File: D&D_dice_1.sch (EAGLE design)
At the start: 28 parts, among them IC1 OPA2340U, SW1 SPST_SWITCH, SW2 SPST_SWITCH, SW3 SPST_SWITCH, SW4 SPST_SWITCH, SW5 SPST_SWITCH, SW6 SPST_SWITCH, U1 ATMEGA168

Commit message: Board, code improvement.
Optimized the code, and improved the board a bit.
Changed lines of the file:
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@@
 <instance part="P+4" gate="1" x="132.08" y="154.94"/>
 <instance part="GND6" gate="1" x="45.72" y="144.78"/>
-<instance part="U$3" gate="G$1" x="160.02" y="45.72"/>
+<instance part="U$3" gate="G$1" x="15.24" y="15.24"/>
 <instance part="R15" gate="G$1" x="58.42" y="83.82" rot="R90"/>
 <instance part="GND7" gate="1" x="58.42" y="73.66"/>
@@
 <pinref part="Q1" gate="G$1" pin="B"/>
 <wire x1="10.16" y1="149.86" x2="12.7" y2="147.32" width="0.1524" layer="91"/>
+<junction x="10.16" y="149.86"/>
+<junction x="12.7" y="147.32"/>
 </segment>
 </net>
@@
 <pinref part="GND1" gate="1" pin="GND"/>
 <wire x1="17.78" y1="142.24" x2="17.78" y2="139.7" width="0.1524" layer="91"/>
+<junction x="17.78" y="142.24"/>
+<junction x="17.78" y="139.7"/>
 </segment>
 <segment>
@@
 <pinref part="GND2" gate="1" pin="GND"/>
 <wire x1="50.8" y1="172.72" x2="53.34" y2="172.72" width="0.1524" layer="91"/>
+<junction x="50.8" y="172.72"/>
+<junction x="53.34" y="172.72"/>
 </segment>
 <segment>
@@
 <pinref part="U1" gate="G$1" pin="AGND"/>
 <wire x1="134.62" y1="114.3" x2="134.62" y2="116.84" width="0.1524" layer="91"/>
+<junction x="134.62" y="116.84"/>
+<junction x="134.62" y="114.3"/>
+<junction x="134.62" y="111.76"/>
+<junction x="132.08" y="111.76"/>
 </segment>
 <segment>
@@
 <pinref part="GND6" gate="1" pin="GND"/>
 <wire x1="43.18" y1="147.32" x2="45.72" y2="147.32" width="0.1524" layer="91"/>
+<junction x="43.18" y="147.32"/>
+<junction x="45.72" y="147.32"/>
 </segment>
 <segment>
@@
 <pinref part="C1" gate="G$1" pin="1"/>
 <wire x1="17.78" y1="152.4" x2="22.86" y2="152.4" width="0.1524" layer="91"/>
+<junction x="17.78" y="152.4"/>
+<junction x="22.86" y="152.4"/>
+<junction x="17.78" y="162.56"/>
 </segment>
 </net>
@@
 <pinref part="U$1" gate="G$1" pin="K"/>
 <wire x1="10.16" y1="162.56" x2="10.16" y2="160.02" width="0.1524" layer="91"/>
+<junction x="10.16" y="160.02"/>
+<junction x="10.16" y="162.56"/>
 </segment>
 </net>
@@
 <wire x1="40.64" y1="137.16" x2="35.56" y2="142.24" width="0.1524" layer="91"/>
 <wire x1="35.56" y1="142.24" x2="35.56" y2="152.4" width="0.1524" layer="91"/>
+<junction x="35.56" y="152.4"/>
+<junction x="30.48" y="152.4"/>
+<junction x="38.1" y="152.4"/>
 </segment>
 </net>
@@
 <wire x1="50.8" y1="137.16" x2="55.88" y2="142.24" width="0.1524" layer="91"/>
 <wire x1="55.88" y1="142.24" x2="55.88" y2="154.94" width="0.1524" layer="91"/>
+<junction x="55.88" y="160.02"/>
+<junction x="55.88" y="154.94"/>
 </segment>
 </net>
@@
 <wire x1="38.1" y1="167.64" x2="55.88" y2="167.64" width="0.1524" layer="91"/>
 <wire x1="55.88" y1="167.64" x2="55.88" y2="165.1" width="0.1524" layer="91"/>
+<junction x="38.1" y="167.64"/>
+<junction x="38.1" y="172.72"/>
+<junction x="40.64" y="172.72"/>
+<junction x="55.88" y="165.1"/>
 </segment>
 </net>
@@
 <wire x1="17.78" y1="172.72" x2="27.94" y2="172.72" width="0.1524" layer="91"/>
 <pinref part="SUPPLY1" gate="1" pin="V+"/>
+<junction x="10.16" y="172.72"/>
+<junction x="17.78" y="172.72"/>
+<junction x="27.94" y="172.72"/>
+<junction x="5.08" y="172.72"/>
 </segment>
 <segment>
@@
 <pinref part="IC1" gate="A" pin="V+"/>
 <wire x1="45.72" y1="162.56" x2="43.18" y2="162.56" width="0.1524" layer="91"/>
+<junction x="43.18" y="162.56"/>
+<junction x="45.72" y="162.56"/>
 </segment>
 <segment>
@@
 <pinref part="C2" gate="G$1" pin="2"/>
 <wire x1="124.46" y1="162.56" x2="129.54" y2="162.56" width="0.1524" layer="91"/>
+<junction x="134.62" y="162.56"/>
+<junction x="134.62" y="160.02"/>
+<junction x="134.62" y="157.48"/>
+<junction x="129.54" y="162.56"/>
 </segment>
 <segment>
@@
 <pinref part="P+3" gate="1" pin="V+"/>
 <wire x1="132.08" y1="177.8" x2="134.62" y2="177.8" width="0.1524" layer="91"/>
+<junction x="132.08" y="177.8"/>
+<junction x="134.62" y="177.8"/>
 </segment>
 <segment>
@@
 <pinref part="U1" gate="G$1" pin="PD7(AIN1)"/>
 <wire x1="182.88" y1="127" x2="185.42" y2="127" width="0.1524" layer="91"/>
-<label x="185.42" y="127" size="2.54" layer="95"/>
+<label x="185.42" y="127" size="1.778" layer="95"/>
 </segment>
 </net>
@@
 <wire x1="134.62" y1="167.64" x2="132.08" y2="167.64" width="0.1524" layer="91"/>
 <pinref part="R7" gate="G$1" pin="1"/>
-</segment>
-</net>
+<junction x="132.08" y="167.64"/>
+<junction x="134.62" y="167.64"/>
+</segment>
+</net>

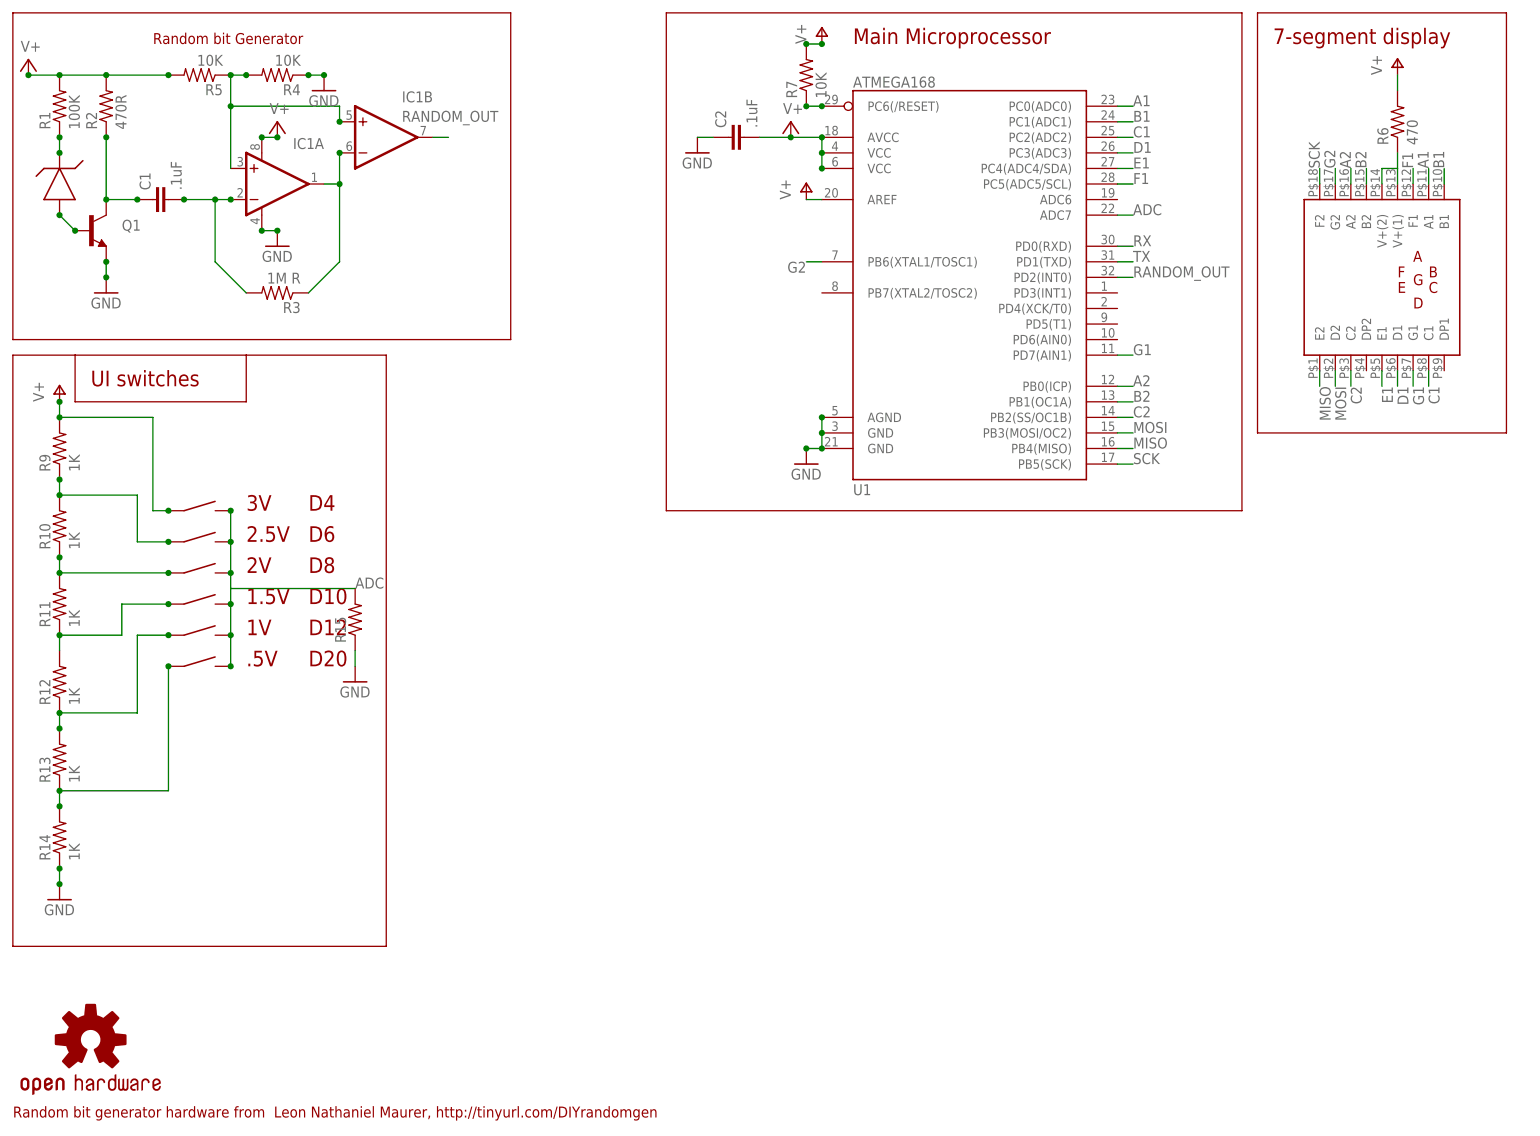
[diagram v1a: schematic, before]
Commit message: Major commit: TESTED
Boards re-jiggered with bigger 0805 pads, because the small ones were
nightmarish. Code also much improved: It now actually works!
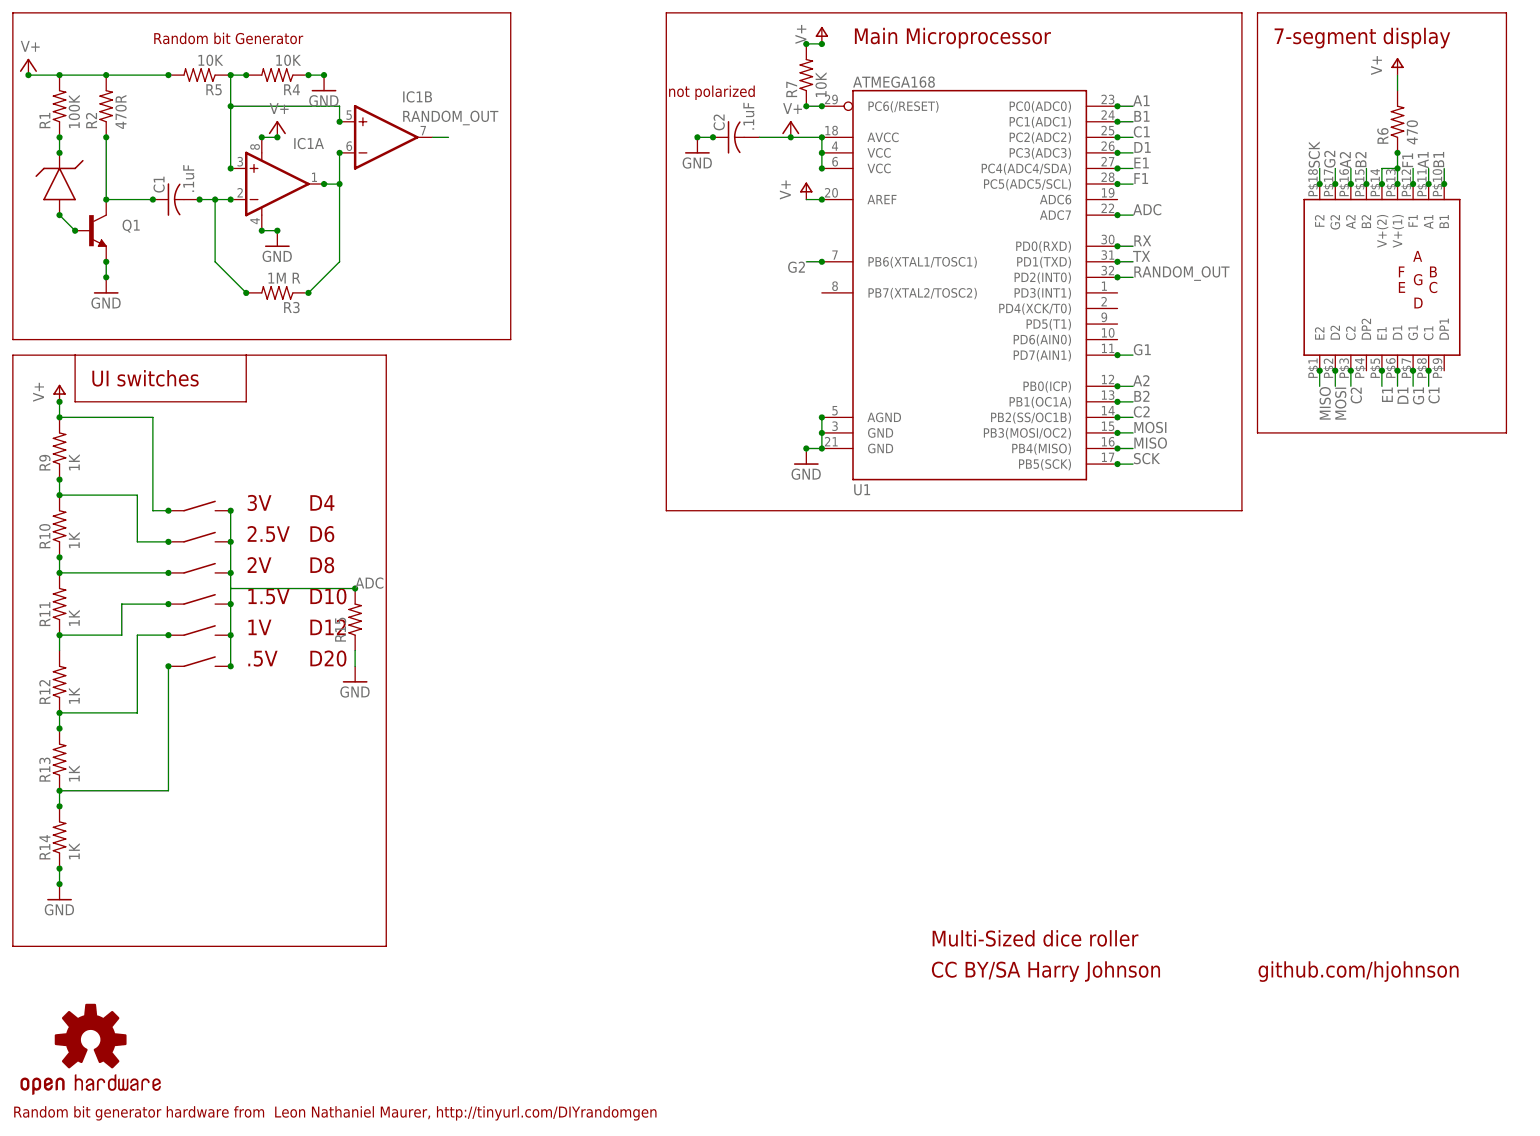
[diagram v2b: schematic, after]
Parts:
- C1, C2: device SparkFun:CAP0805 -> adafruit:C-USC0805
- R1, R10, R11, R12, R13, R14, R15, R2, R4, R5, R6, R7, R9: device SparkFun:RESISTOR0805-RES -> adafruit:R-US_R0805
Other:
- note added: "CC BY/SA Harry Johnson"
- note added: "Multi-Sized dice roller"
- note added: "github.com/hjohnson"
- note added: "not polarized"
- moved on the sheet: C1

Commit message: Added test pads for reset, lightly shifted around a few resistors.
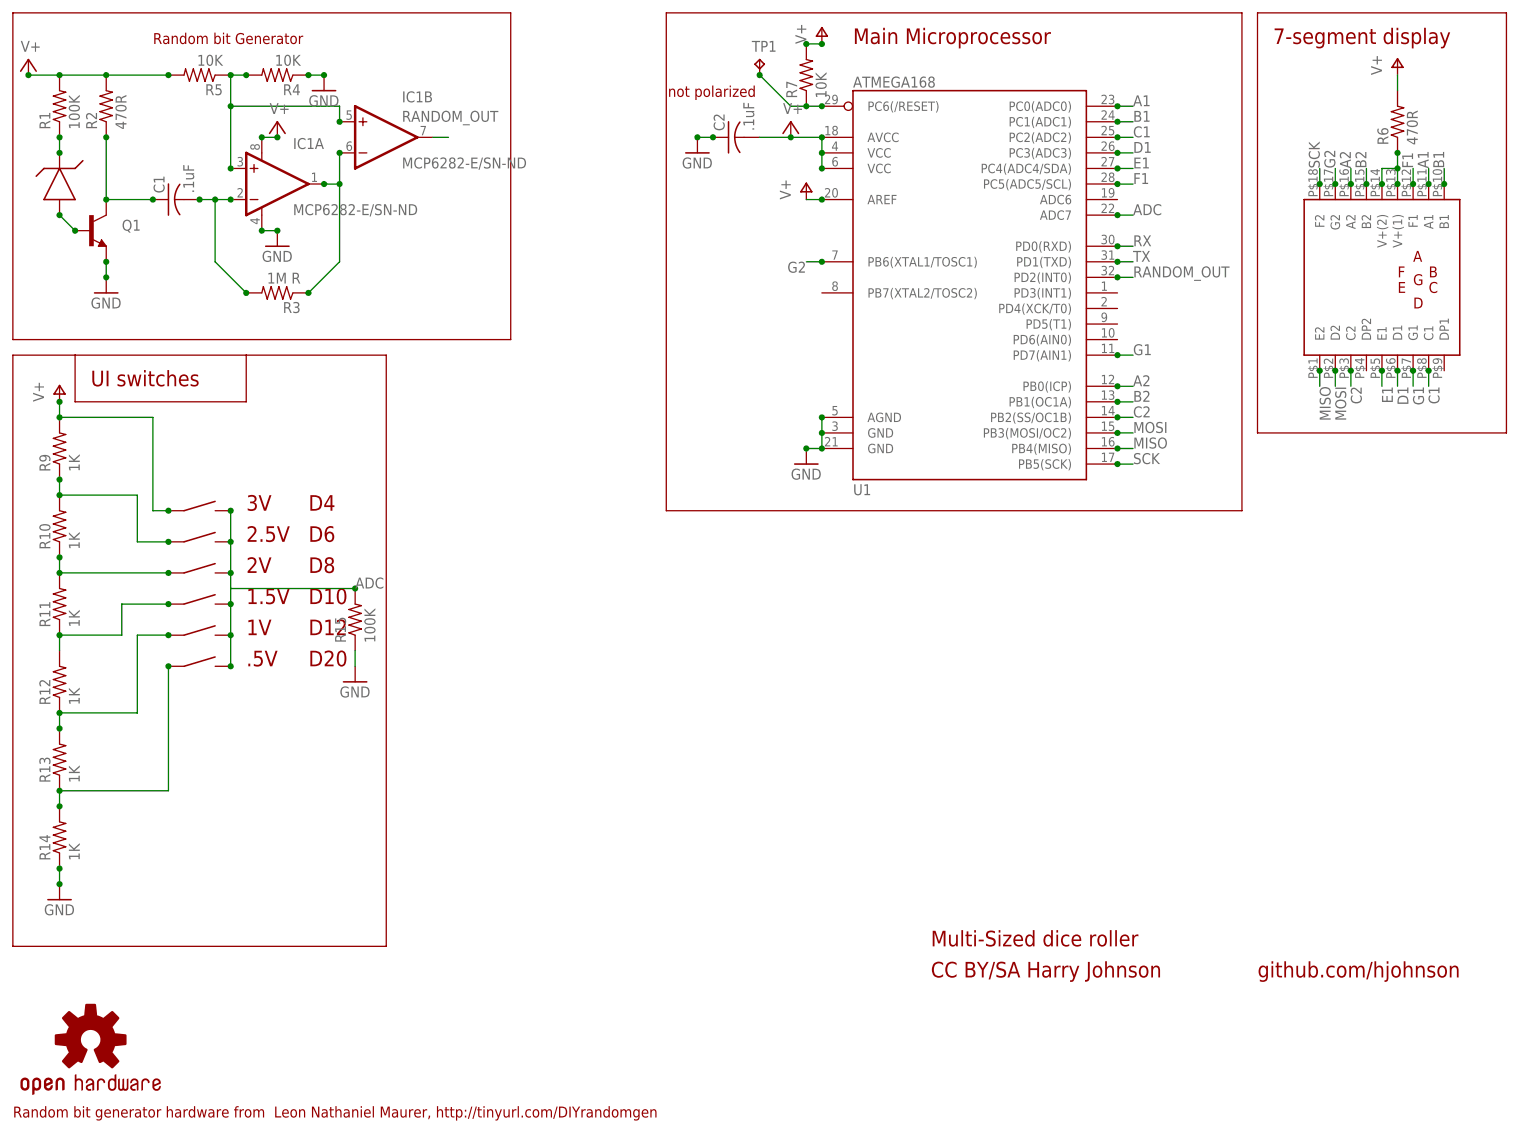
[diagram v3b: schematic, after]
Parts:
- added TP1: TPB1,27, testpad:TPB1,27
- IC1: value OPA2340U -> MCP6282-E/SN-ND
- R15: value (none) -> 100K
- R6: value 470 -> 470R
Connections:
- net /RES: now also TP1.TP
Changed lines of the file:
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@@
 <parts>
 <part name="FRAME1" library="SparkFun" deviceset="FRAME-LETTER" device=""/>
-<part name="IC1" library="burr-brown" deviceset="OPA2340" device="U" value=""/>
+<part name="IC1" library="burr-brown" deviceset="OPA2340" device="U" value="MCP6282-E/SN-ND"/>
 <part name="U$1" library="hjohnson_library" deviceset="ZXRE1004FFTA" device="" value=""/>
 <part name="Q1" library="SparkFun" deviceset="TRANSISTOR_NPN" device="SOT23"/>
@@
 <part name="SUPPLY3" library="supply2" deviceset="V+" device=""/>
 <part name="GND3" library="SparkFun" deviceset="GND" device=""/>
-<part name="R6" library="adafruit" deviceset="R-US_" device="R0805" value="470"/>
+<part name="R6" library="adafruit" deviceset="R-US_" device="R0805" value="470R"/>
 <part name="P+1" library="supply1" deviceset="V+" device=""/>
 <part name="GND4" library="SparkFun" deviceset="GND" device=""/>
@@
 <part name="GND6" library="SparkFun" deviceset="GND" device=""/>
 <part name="U$3" library="SparkFun" deviceset="OSHW-LOGO" device="S"/>
-<part name="R15" library="adafruit" deviceset="R-US_" device="R0805"/>
+<part name="R15" library="adafruit" deviceset="R-US_" device="R0805" value="100K"/>
 <part name="GND7" library="SparkFun" deviceset="GND" device=""/>
+<part name="TP1" library="testpad" deviceset="TP" device="B1,27"/>
 </parts>
 <sheets>
@@
 <instance part="R15" gate="G$1" x="58.42" y="83.82" rot="R90"/>
 <instance part="GND7" gate="1" x="58.42" y="73.66"/>
+<instance part="TP1" gate="G$1" x="124.46" y="175.26"/>
 </instances>
 <busses>
@@
 <junction x="132.08" y="167.64"/>
 <junction x="134.62" y="167.64"/>
-</segment>
-</net>
+<pinref part="TP1" gate="G$1" pin="TP"/>
+<wire x1="124.46" y1="172.72" x2="129.54" y2="167.64" width="0.1524" layer="91"/>
+<wire x1="129.54" y1="167.64" x2="132.08" y2="167.64" width="0.1524" layer="91"/>
+<junction x="124.46" y="172.72"/>
+</segment>
+</net>
